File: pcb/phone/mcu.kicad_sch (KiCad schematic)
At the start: 25 parts, among them J3 Conn_01x04, U1 STM32H743ZIT6, Y1 ECS-80-12-33Q-GN-TR

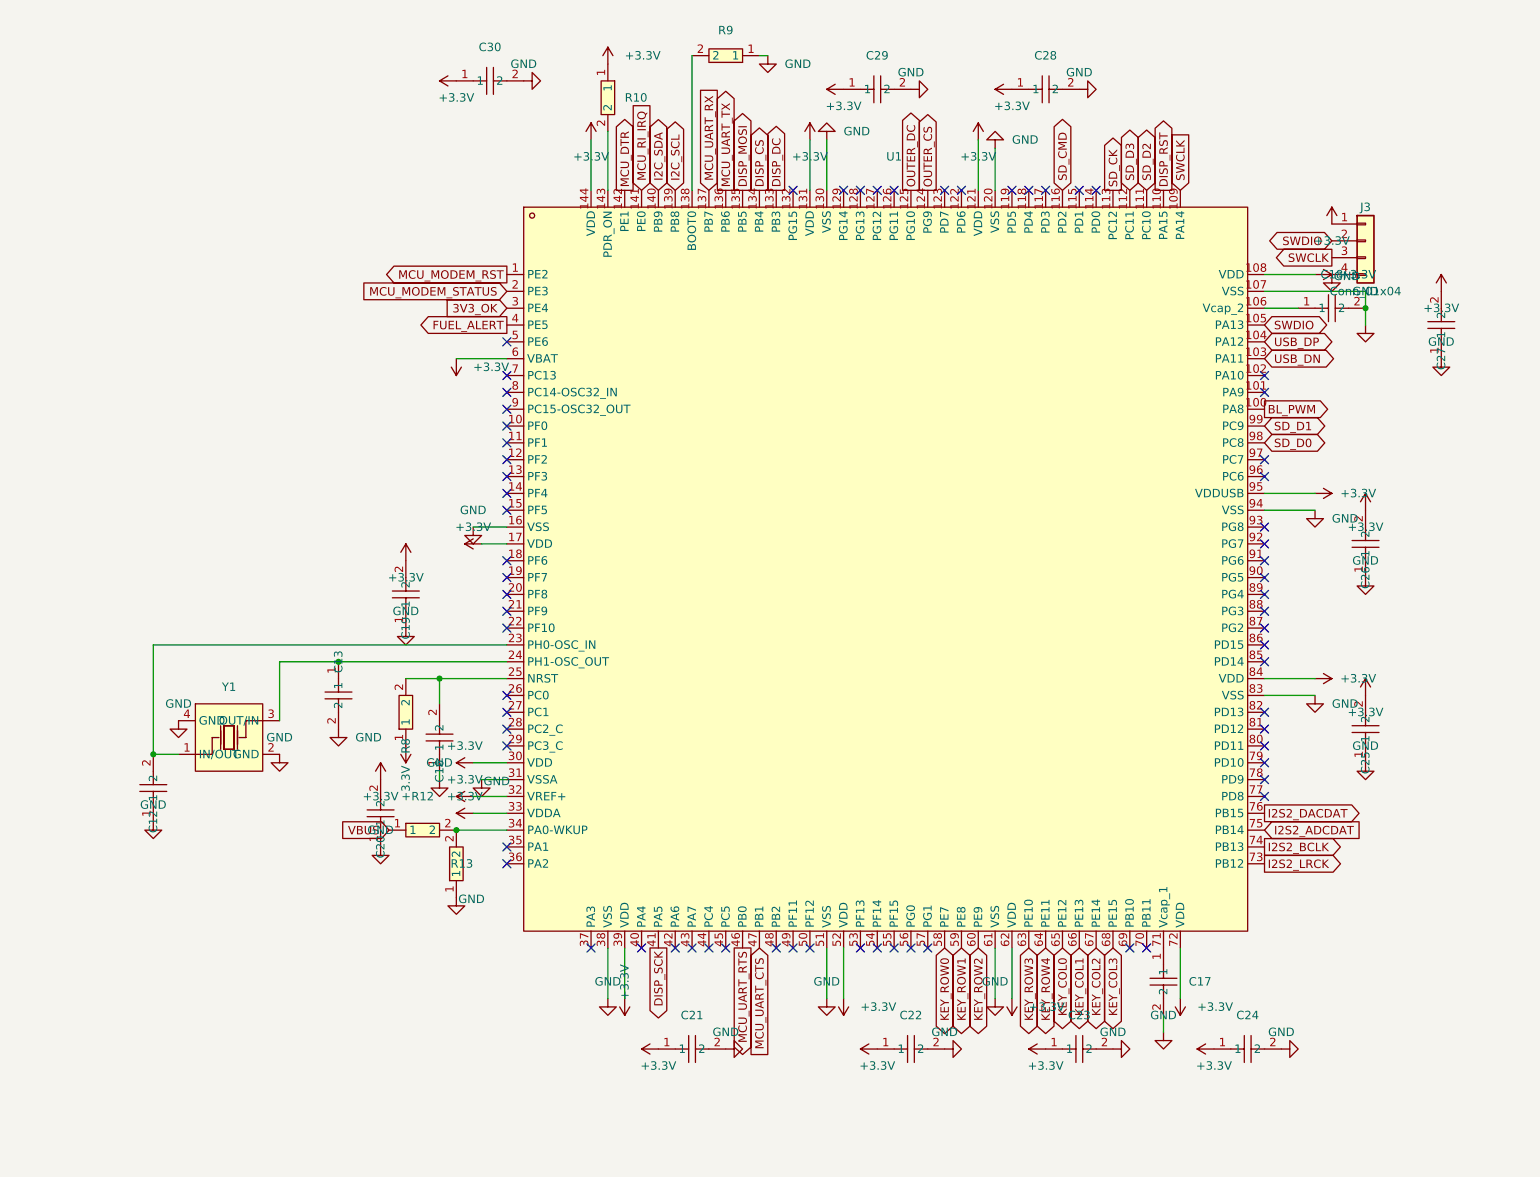
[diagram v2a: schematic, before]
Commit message: Cleanup: remove rejected part symbols, one-off scripts, stale datasheets
- Remove 7 rejected symbols from easyeda2kicad.kicad_sym (PJ-327C-4A,
  PJ-3250-5A, PJ-3240-5A, TYPE-C16PLC-H10.0, PJ-327A5JJ, PJ-327-P5,
  TYPEC-306DDW-ARP16) — replaced by Tensility 54-00298 and GCT USB4085-GF-A
- Delete 10 one-off inspection scripts (check_*.py, find_*.py, dump_*.py,
  extract_*.py) — keep only gen_*.py schematic generators
- Delete rejected datasheets (pj3126-5a, pj3240-5a, pj3250-5a, pj3f07-5p,
  N114 superseded display)
- Delete generated BOM/POS CSV files
- Add alps-ssss2.pdf and gct-usb4085.pdf to reference README index
- Include all schematic changes from previous sessions (SD pullups, VBUS
  divider fix, level shifter verification, codec caps, DCVDD fix)

Generated with [Devin](https://devin.ai)

Co-Authored-By: Devin <158243242+devin-ai-integration[bot]@users.noreply.github.com>
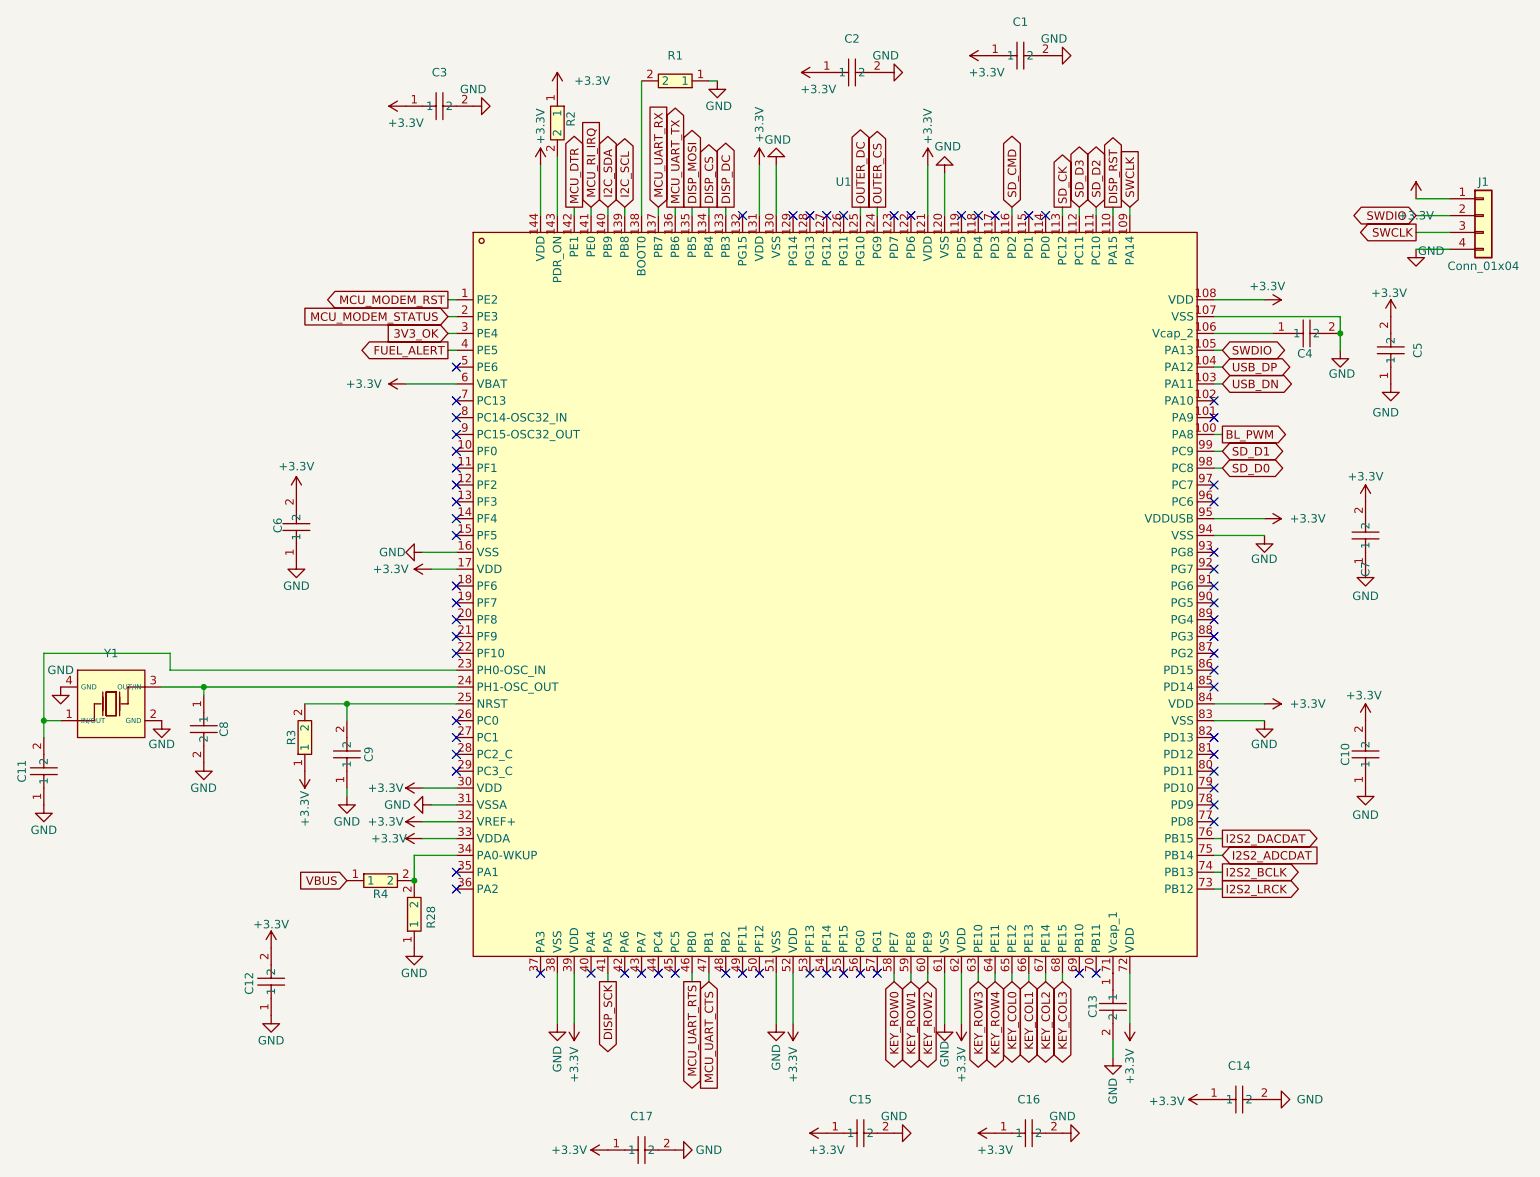
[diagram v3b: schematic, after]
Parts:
- removed R13: 47k, easyeda2kicad:R0603, symbol passives:RC0603JR-0710KL
- added R28: RC0603FR-0768KL, easyeda2kicad:R0603, symbol passives:RC0603FR-0768KL
- renumbered C28 to C1, C25 to C10, C12 to C11, C20 to C12, C17 to C13, C24 to C14, C22 to C15, C23 to C16, C21 to C17, C29 to C2, C30 to C3, C18 to C4, C27 to C5, C19 to C6, C26 to C7, C13 to C8, C16 to C9, J3 to J1, R9 to R1, R10 to R2, R8 to R3, R12 to R4
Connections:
- net GND: now also R28.1
- net at R4.2, U1.34 (PA0-WKUP): now also R28.2
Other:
- moved on the sheet: C1, C10, C11, C12, C13, C14, C15, C16, C17, C2, C3, C4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
